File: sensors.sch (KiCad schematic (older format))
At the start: 11 parts

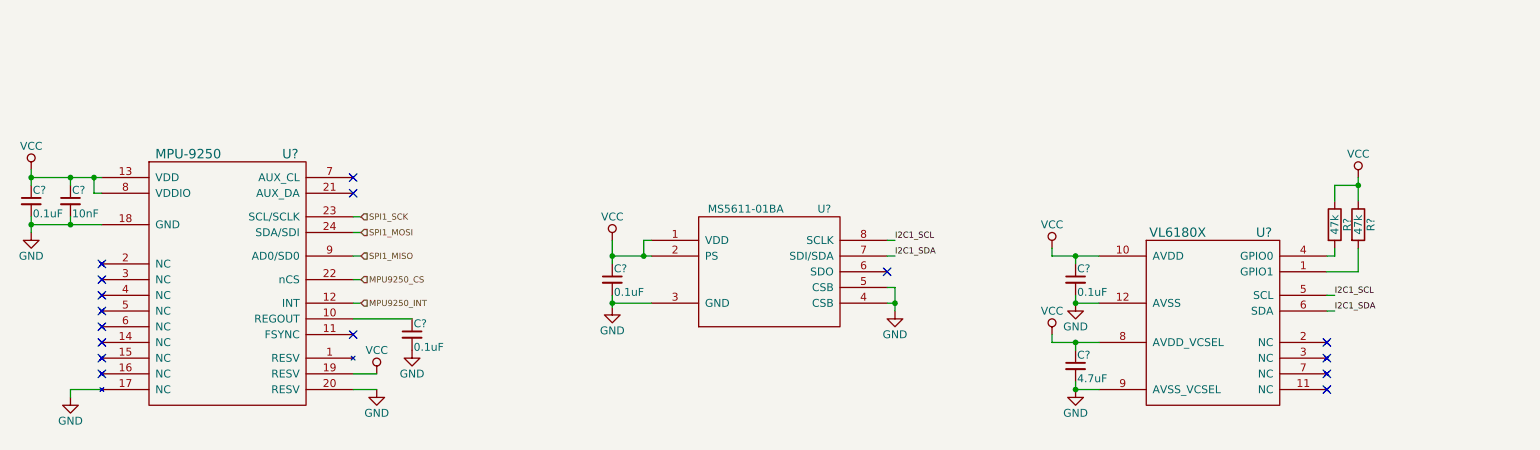
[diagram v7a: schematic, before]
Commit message: Add IR Leds on top and bottom with enable on MCU
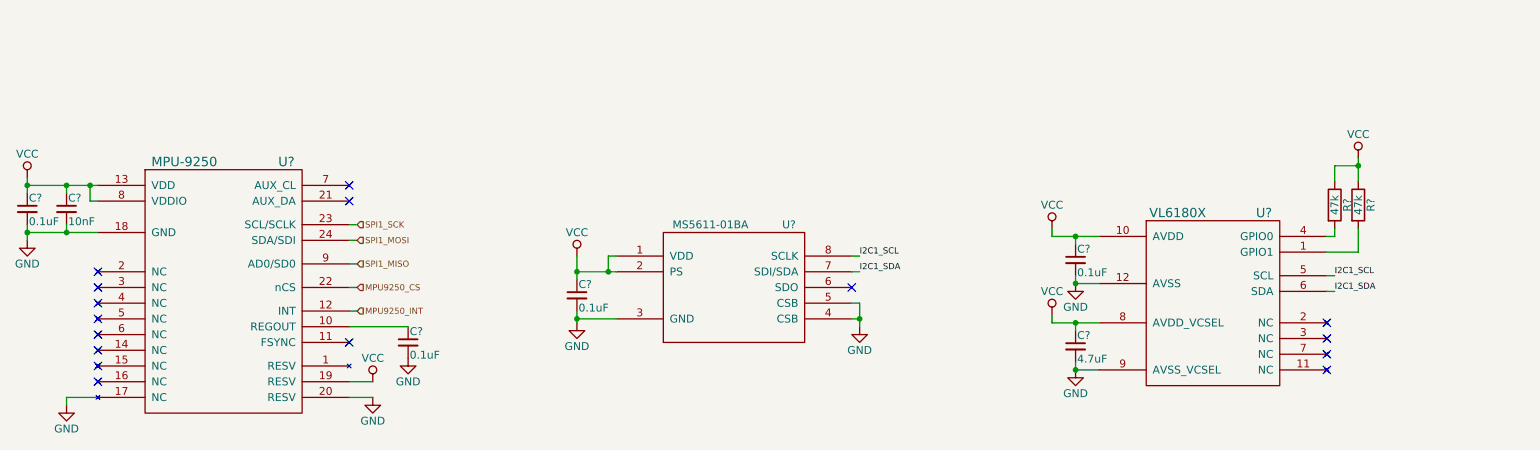
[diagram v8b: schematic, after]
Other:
- moved on the sheet: C?, R?, U?
